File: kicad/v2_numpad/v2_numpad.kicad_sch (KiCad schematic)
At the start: 45 parts, among them J1 Conn_02x08_Top_Bottom

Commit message: [kicad] rename and update numpad kicad project
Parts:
- D_CapsLock1: renamed from D_CapsLock; footprint (none) -> mantyl:SK6812-MINI-E
- D_Keymap1: renamed from D_Keymap; footprint (none) -> mantyl:SK6812-MINI-E
- D_NumLock1: renamed from D_NumLock; footprint (none) -> mantyl:SK6812-MINI-E
- D_Power1: renamed from D_Power; footprint (none) -> mantyl:SK6812-MINI-E
- D_ScrollLock1: renamed from D_ScrollLock; footprint (none) -> mantyl:SK6812-MINI-E
- SW_Dot1: renamed from SW_Dot; footprint (none) -> mantyl:Kailh_socket_MX_platemount
- SW_Enter1: renamed from SW_Enter; footprint (none) -> mantyl:Kailh_socket_MX_platemount
- SW_Extra1: renamed from SW_Extra; footprint (none) -> mantyl:Kailh_socket_MX_platemount
- SW_Minus1: renamed from SW_Minus; footprint (none) -> mantyl:Kailh_socket_MX_platemount
- SW_NP0, SW_NP1, SW_NP2, SW_NP3, SW_NP4, SW_NP5, SW_NP6, SW_NP7, SW_NP8, SW_NP9: footprint (none) -> mantyl:Kailh_socket_MX_platemount
- SW_Plus1: renamed from SW_Plus; footprint (none) -> mantyl:Kailh_socket_MX_platemount
- SW_Slash1: renamed from SW_Slash; footprint (none) -> mantyl:Kailh_socket_MX_platemount
- SW_Star1: renamed from SW_Star; footprint (none) -> mantyl:Kailh_socket_MX_platemount
- renumbered D14 to D12, D7 to D13, D8 to D14, D9 to D15, D17 to D16, D18 to D17, D3 to D2, D4 to D3, D16 to D4, D12 to D6, D13 to D7, D15 to D8, D6 to D9
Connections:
- net R9 is gone; now on net LED_Data: J1.12 (Pin_12)
- net GND: now also D_CapsLock1.3 (VSS), D_Keymap1.3 (VSS), D_NumLock1.3 (VSS), D_Power1.3 (VSS), D_ScrollLock1.3 (VSS); no longer D_CapsLock1.1 (VSS), D_Keymap1.1 (VSS), D_NumLock1.1 (VSS), D_Power1.1 (VSS), D_ScrollLock1.1 (VSS)
- net LED_Data: now also D_ScrollLock1.4 (DIN); no longer D_ScrollLock1.2 (DIN)
- net at D_CapsLock1.2 (DOUT): now also D_NumLock1.4 (DIN); no longer D_ScrollLock1.4 (DOUT)
- net at D_Power1.2 (DOUT): no longer D_Keymap1.4 (DOUT)
- net at D_Power1.4 (DIN): now also D_Keymap1.2 (DOUT)
- net at D_CapsLock1.4 (DIN): now also D_ScrollLock1.2 (DOUT); no longer D_NumLock1.2 (DIN)
- net R10: no longer names the net of J1.13 (Pin_13)
- net R11: no longer names the net of J1.14 (Pin_14)
- net V_LED renamed +5V
- net +5V: now also D_CapsLock1.1 (VDD), D_Keymap1.1 (VDD), D_NumLock1.1 (VDD), D_Power1.1 (VDD), D_ScrollLock1.1 (VDD); no longer D_CapsLock1.3 (VDD), D_Keymap1.3 (VDD), D_NumLock1.3 (VDD), D_Power1.3 (VDD), D_ScrollLock1.3 (VDD)
- new net: D_Keymap1.4 (DIN), D_NumLock1.2 (DOUT)
- no-connect marks 0 -> 3

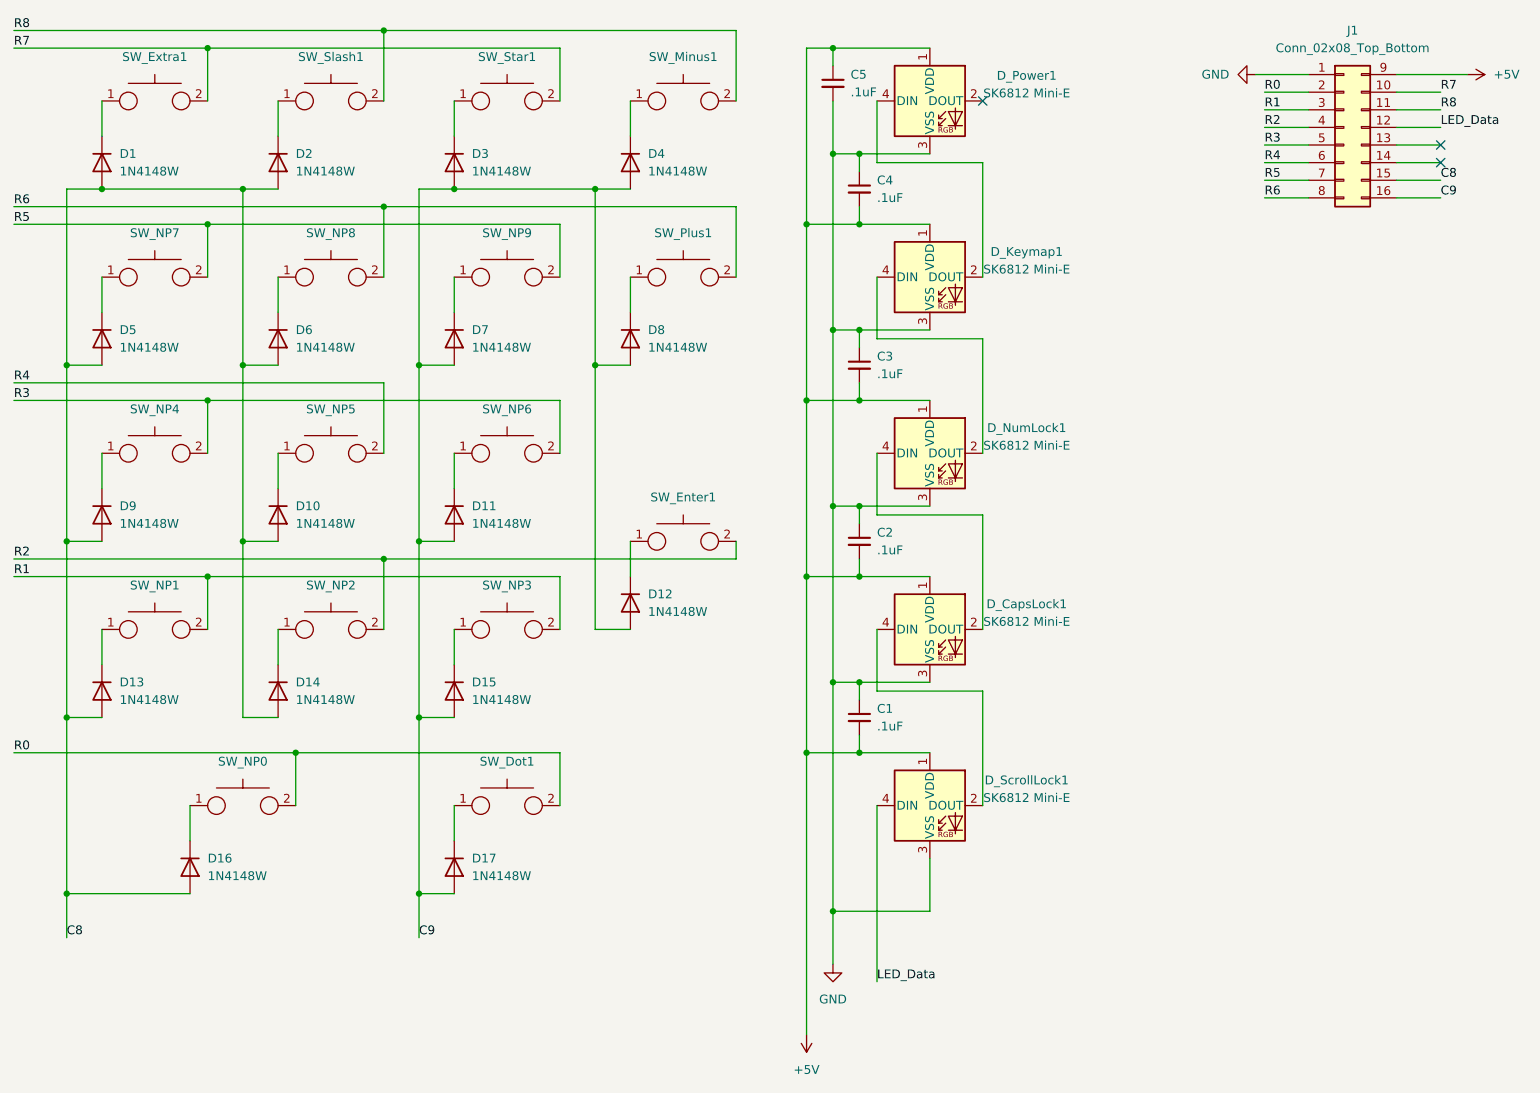
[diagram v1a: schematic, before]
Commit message: [kicad] numpad work in progress
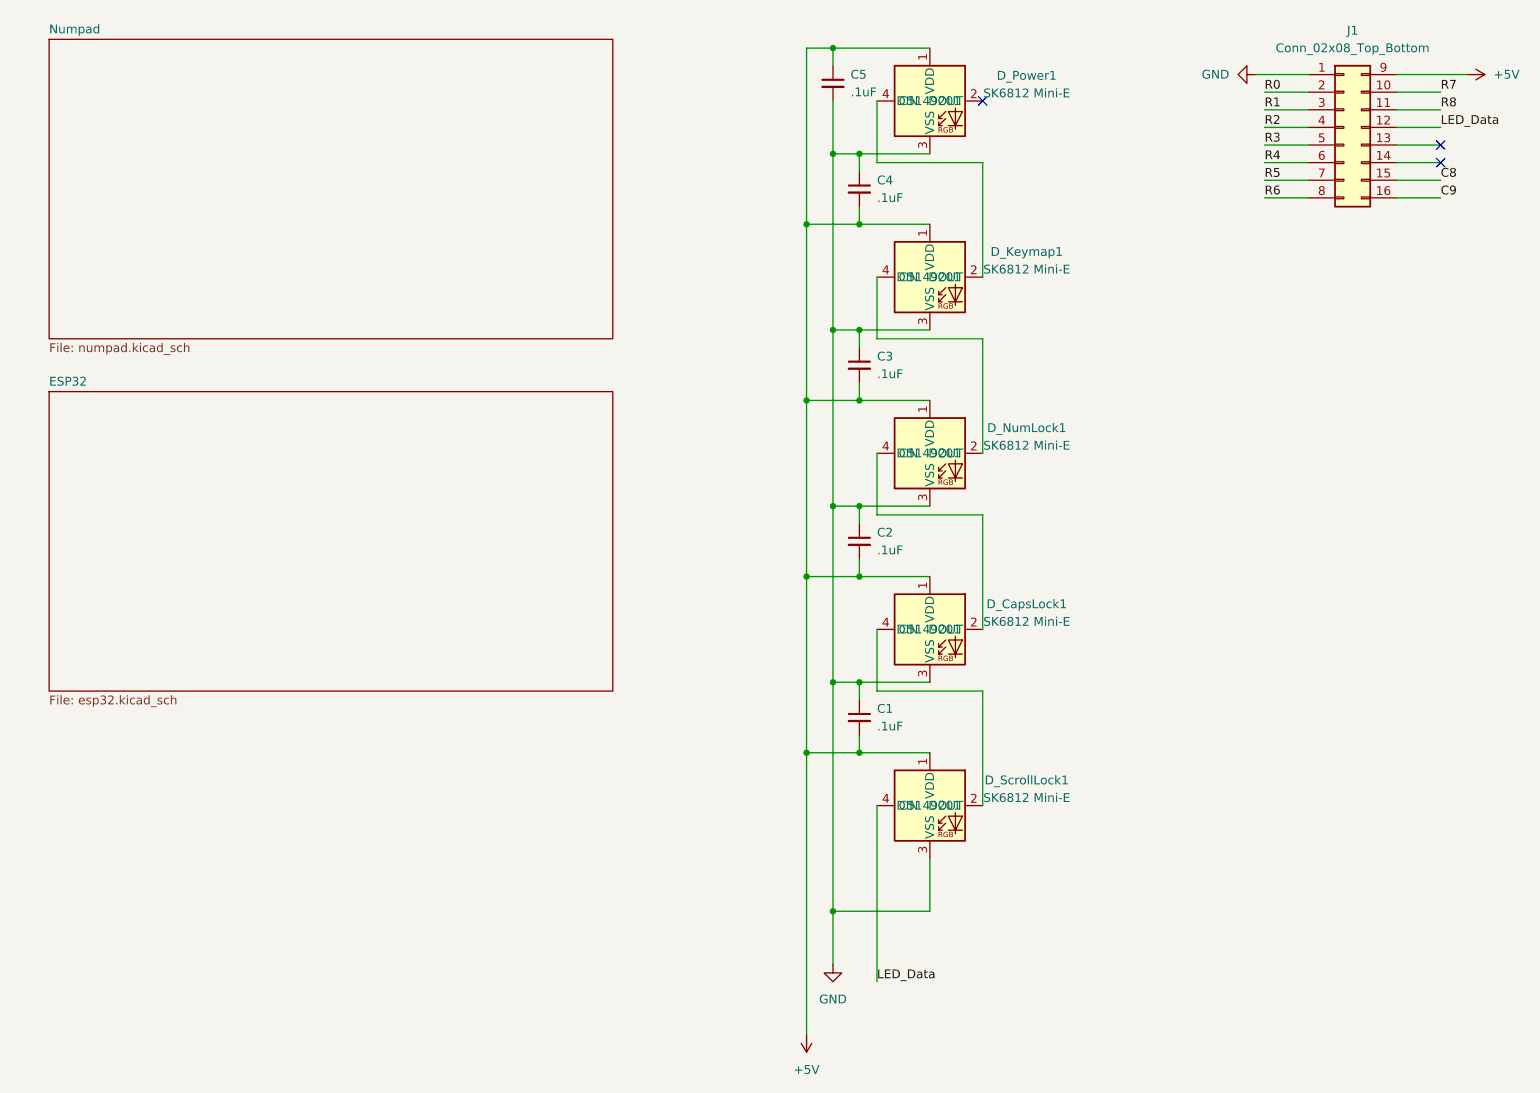
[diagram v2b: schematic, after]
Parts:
- removed D1, D10, D11, D12, D13, D14, D15, D16, D17, D2, D3, D4, D5, D6, D7, D8, D9: 1N4148W, Diode_SMD:D_SOD-123, symbol Diode:1N4148W
- removed SW_Dot1, SW_Enter1, SW_Extra1, SW_Minus1, SW_NP0, SW_NP1, SW_NP2, SW_NP3, SW_NP4, SW_NP5, SW_NP6, SW_NP7, SW_NP8, SW_NP9, SW_Plus1, SW_Slash1, SW_Star1: ~, mantyl:Kailh_socket_MX_platemount, symbol mantyl:Kailh_MX_Socket
- D_CapsLock1, D_Keymap1, D_NumLock1, D_Power1, D_ScrollLock1: JLCPCB Part (none) -> C5149201
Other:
- added sheet ESP32 (esp32.kicad_sch)
- added sheet Numpad (numpad.kicad_sch)

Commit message: [kicad] some more minor tweaks to the numpad
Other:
- added sheet CP2102N (cp2102n.kicad_sch)
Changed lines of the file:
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@@
       (effects (font (size 1.27 1.27)) (justify left top) hide)
     )
-    (property "JLCPCB Part" "C5149201" (at 157.48 139.7 0)
-      (effects (font (size 1.27 1.27)))
+    (property "JLCPCB Part" "C5149201" (at 163.83 153.67 0)
+      (effects (font (size 1.27 1.27)) hide)
     )
     (pin "1")
@@
       (effects (font (size 1.27 1.27)) (justify left top) hide)
     )
-    (property "JLCPCB Part" "C5149201" (at 157.48 38.1 0)
-      (effects (font (size 1.27 1.27)))
+    (property "JLCPCB Part" "C5149201" (at 163.83 52.07 0)
+      (effects (font (size 1.27 1.27)) hide)
     )
     (pin "1")
@@
       (effects (font (size 1.27 1.27)) (justify left top) hide)
     )
-    (property "JLCPCB Part" "C5149201" (at 157.48 114.3 0)
-      (effects (font (size 1.27 1.27)))
+    (property "JLCPCB Part" "C5149201" (at 163.83 128.27 0)
+      (effects (font (size 1.27 1.27)) hide)
     )
     (pin "1")
@@
       (effects (font (size 1.27 1.27)) (justify left top) hide)
     )
-    (property "JLCPCB Part" "C5149201" (at 157.48 88.9 0)
-      (effects (font (size 1.27 1.27)))
+    (property "JLCPCB Part" "C5149201" (at 163.83 102.87 0)
+      (effects (font (size 1.27 1.27)) hide)
     )
     (pin "1")
@@
       (effects (font (size 1.27 1.27)) (justify left top) hide)
     )
-    (property "JLCPCB Part" "C5149201" (at 157.48 63.5 0)
-      (effects (font (size 1.27 1.27)))
+    (property "JLCPCB Part" "C5149201" (at 163.83 77.47 0)
+      (effects (font (size 1.27 1.27)) hide)
     )
     (pin "1")
@@
       )
     )
+  )
+  (sheet (at 30.48 130.81) (size 81.28 43.18) (fields_autoplaced)
+    (stroke (width 0.1524) (type solid))
+    (fill (color 0 0 0 0.0000))
+    (property "Sheetname" "CP2102N" (at 30.48 130.0984 0)
+      (effects (font (size 1.27 1.27)) (justify left bottom))
+    )
+    (property "Sheetfile" "cp2102n.kicad_sch" (at 30.48 174.5746 0)
+      (effects (font (size 1.27 1.27)) (justify left top))
+    )
+    (instances
+      (project "v2_numpad"
+        (path "/42eee74c-d04d-4a1d-8e02-a7aca1694734" (page "4"))
+      )
+    )
